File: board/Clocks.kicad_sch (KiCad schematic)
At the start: 21 parts, among them J10 Front Panel, J11 ATX-24, J5 0.89489MHz, J6 1.78977MHz, J7 3.57955MHz, J8 7.15909MHz, U39 74ACT14, U40 74F191, U43 DM1813-10, Y1 14.31818MHz

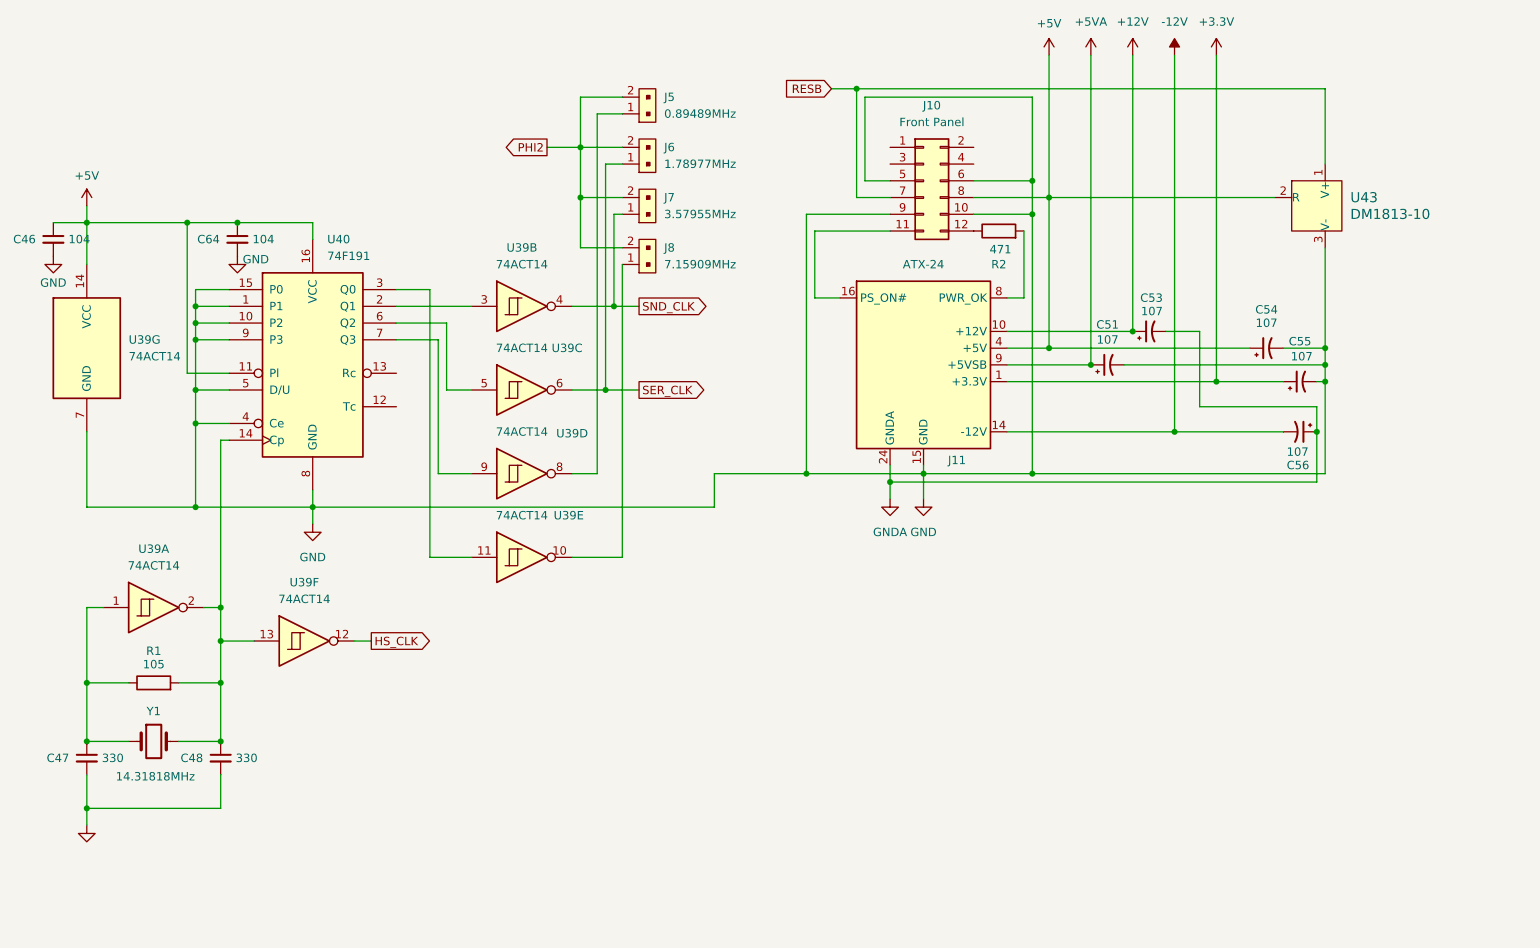
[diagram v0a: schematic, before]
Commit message: Board V1.8D: reliability changes only, the same software as 1.8C
CMOS highs into the W65C02S: U11 (its clock), U22 (IRQB) and U59 (its data bus) are 74ACT parts.
Decoupling at the sound chips and op-amps; four 47 uF bulk capacitors on +5 V; GNDA joined to GND once,
by the YM3012 (R29). Series terminations on the clocks (R23-R27, each driver's net X_SRC) and on the
crystal's drive (R22). A fixed pull-up on RDY (R28); pull-ups on the data bus (RN4: an empty slot reads
$FF). U26's spare half placed and disabled, and U22's spare inputs tied low. ATX pin 20 feeds the slots'
-5V. The ACIA's CTS through a jumper (J30: 1-2 as 1.8C, 2-3 always on). Loose wires removed, no-connects
marked, the root sheet's boxes tidied, and every sheet's revision set to 1.8D. The netlist differs from
1.8C's only by these (checked net by net); ERC finds nothing new. board/CHANGES-1.8D.md lists them. The
PCB isn't updated yet.

Co-Authored-By: Claude Opus 5.5 <noreply@anthropic.com>
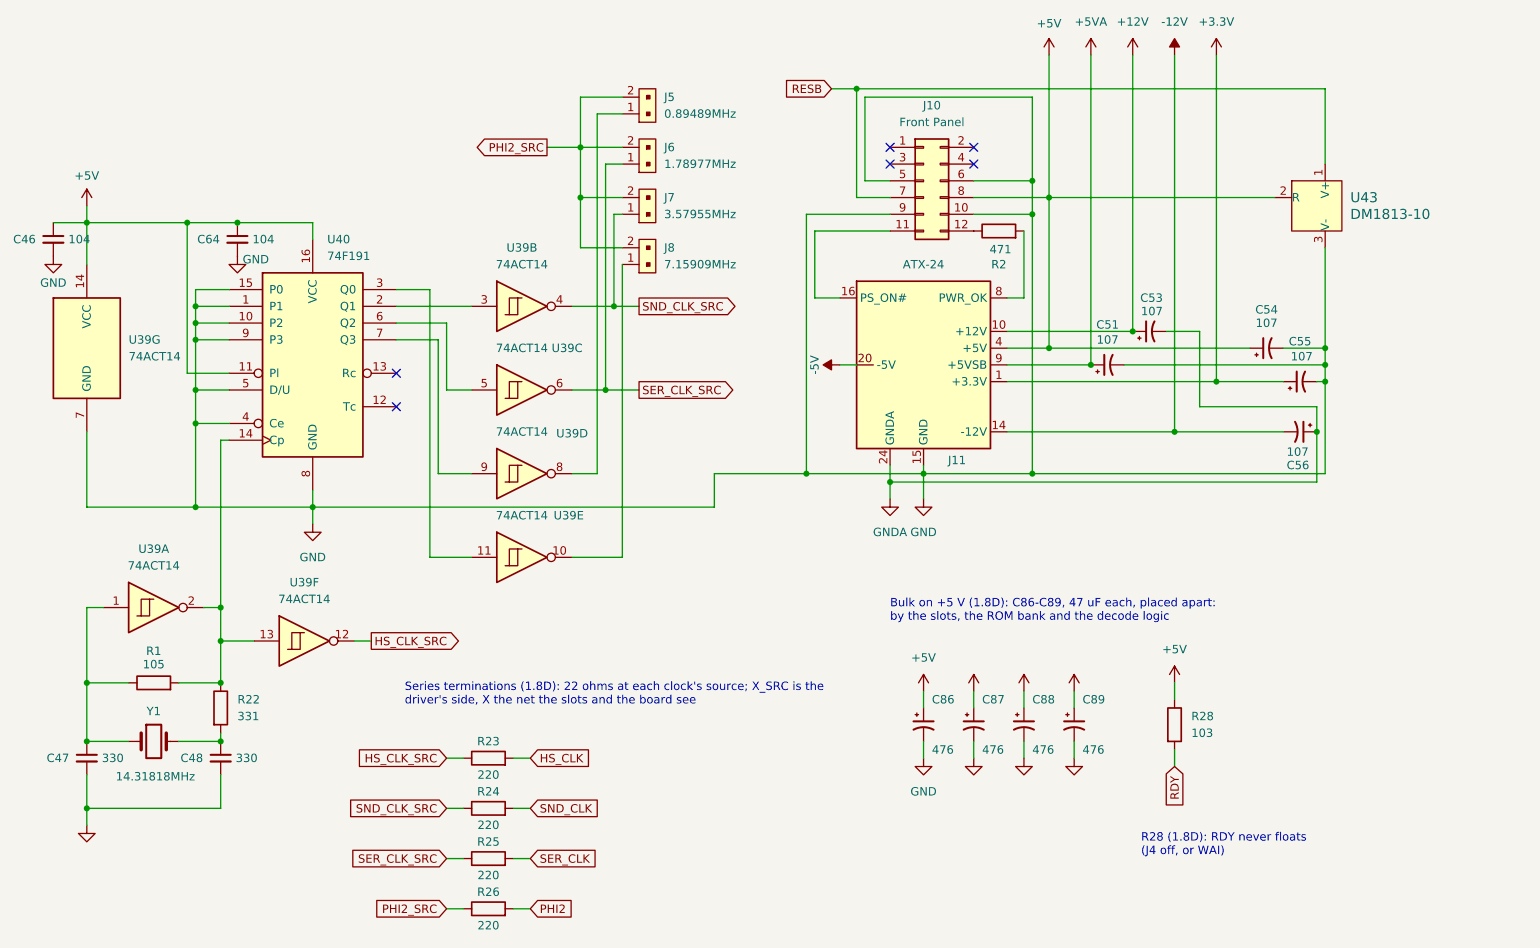
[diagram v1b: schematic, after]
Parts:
- added C86, C87, C88, C89: 476, Capacitor_THT:CP_Radial_D6.3mm_P2.50mm, symbol Device:C_Polarized_Small_US
- added R22: 331, Resistor_THT:R_Axial_DIN0204_L3.6mm_D1.6mm_P5.08mm_Horizontal, symbol Device:R
- added R23, R24, R25, R26: 220, Resistor_THT:R_Axial_DIN0204_L3.6mm_D1.6mm_P5.08mm_Horizontal, symbol Device:R
- added R28: 103, Resistor_THT:R_Axial_DIN0204_L3.6mm_D1.6mm_P5.08mm_Horizontal, symbol Device:R
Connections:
- net +5V: now also C86.1, C87.1, C88.1, C89.1, R28.1
- net GND: now also C86.2, C87.2, C88.2, C89.2
- net HS_CLK: now also R23.2; no longer U39.12
- net PHI2: now also R26.2; no longer J5.2, J6.2, J7.2, J8.2
- net SER_CLK: now also R25.2; no longer J6.1, U39.6
- net SND_CLK: now also R24.2; no longer J7.1, U39.4
- net at R1.2, U39.13, U39.2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: now also R22.1; no longer C48.1, Y1.2
- net -5V: now reaches J11.20 (-5V)
- new net: C48.1, R22.2, Y1.2
- new net HS_CLK_SRC: R23.1, U39.12
- new net PHI2_SRC: J5.2, J6.2, J7.2, J8.2, R26.1
- new net RDY: R28.2
- new net SER_CLK_SRC: J6.1, R25.1, U39.6
- new net SND_CLK_SRC: J7.1, R24.1, U39.4
- no-connect marks 0 -> 6
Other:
- note added: "Bulk on +5 V (1.8D): C86-C89, 47 uF each, placed apart: by the slots, the ROM bank and the decode logic"
- note added: "R28 (1.8D): RDY never floats (J4 off, or WAI)"
- note added: "Series terminations (1.8D): 22 ohms at each clock's source; X_SRC is the driver's side, X the net the slots and the board see"

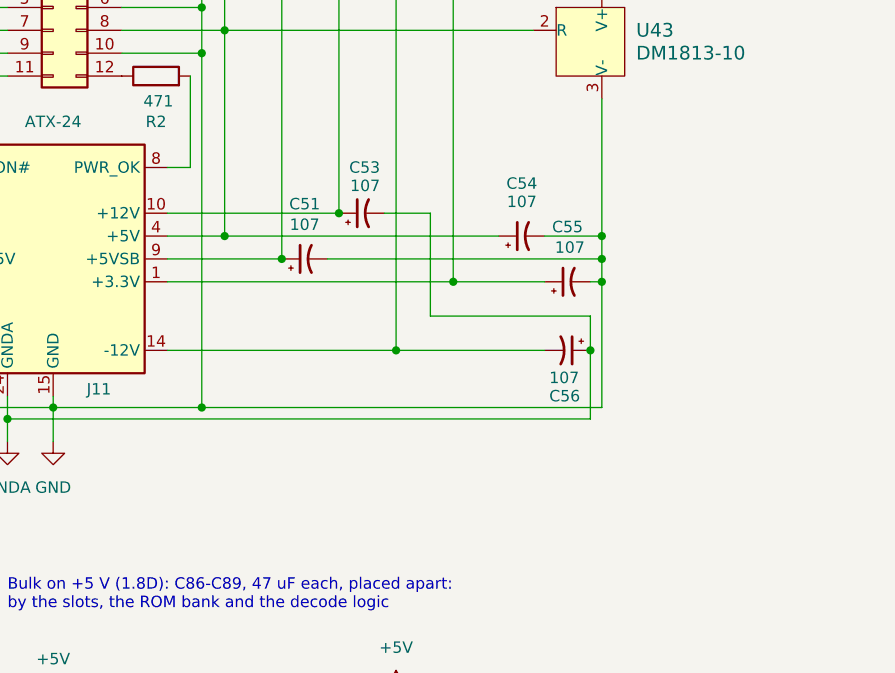
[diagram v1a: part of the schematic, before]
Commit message: Board V1.8D: the power LED (J10 pin 12, R2) lit from +5 V, not from the ATX supply's PWR_OK
PWR_OK is a logic signal; the main +5 V rail is up only while the supply is on, so the LED means the same.
PWR_OK is marked unconnected. The netlist's only change: R2 pin 2 from PWR_OK to +5V.

Co-Authored-By: Claude Opus 5.5 <noreply@anthropic.com>
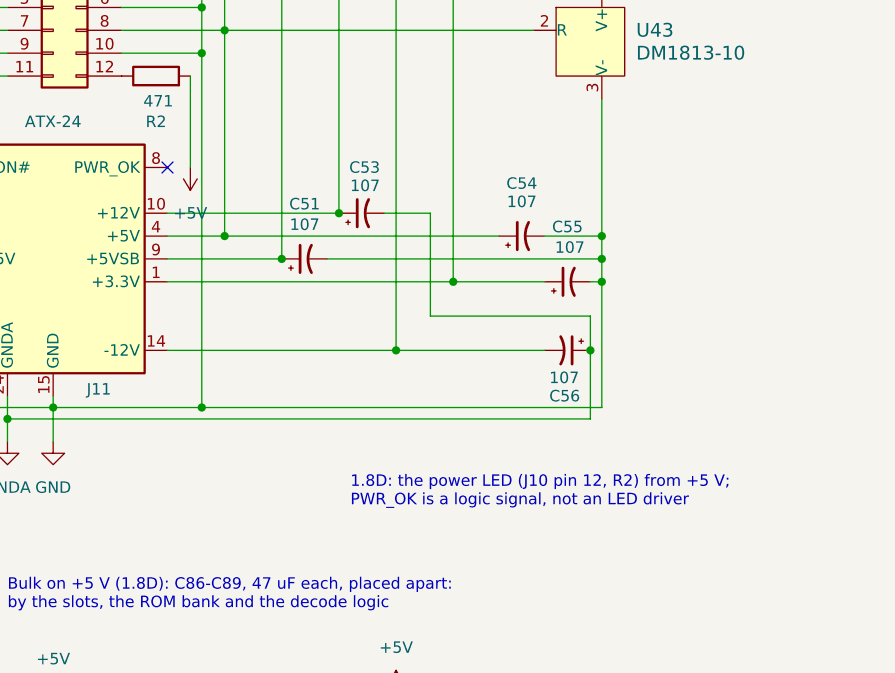
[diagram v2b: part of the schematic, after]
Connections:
- net +5V: now also R2.2
- net at J11.8 (PWR_OK): no longer R2.2
- no-connect marks 6 -> 7
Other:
- note added: "1.8D: the power LED (J10 pin 12, R2) from +5 V; PWR_OK is a logic signal, not an LED driver"
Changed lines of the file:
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@@
 	(wire
 		(pts
-			(xy 185.42 82.55) (xy 187.96 82.55)
-		)
-		(stroke
-			(width 0)
-			(type default)
-		)
-	)
-	(wire
-		(pts
 			(xy 99.06 109.22) (xy 104.14 109.22)
 		)
@@
 	(no_connect (at 167.64 62.23))
 	(no_connect (at 180.34 62.23))
+	(symbol
+		(lib_id "power:+5V")
+		(at 187.96 82.55 180)
+		(unit 1)
+		(exclude_from_sim no)
+		(in_bom yes)
+		(on_board yes)
+		(dnp no)
+		(property "Reference" "#PWR0111"
+			(at 187.96 82.55 0)
+			(effects
+				(font (size 1.27 1.27))
+				hide
+			)
+		)
+		(property "Value" "+5V"
+			(at 187.96 87.63 0)
+			(effects
+				(font (size 1.27 1.27))
+			)
+		)
+		(property "Footprint" ""
+			(at 187.96 82.55 0)
+			(effects
+				(font (size 1.27 1.27))
+				hide
+			)
+		)
+		(property "Datasheet" ""
+			(at 187.96 82.55 0)
+			(effects
+				(font (size 1.27 1.27))
+				hide
+			)
+		)
+		(pin "1")
+		(instances
+			(project ""
+				(path "/ef29fc71-3fec-48b5-8a1a-46bee537a98c/9a593a77-f18f-43cb-9fdd-893618b7b90a"
+					(reference "#PWR0111")
+					(unit 1)
+				)
+			)
+		)
+	)
+	(no_connect (at 185.42 82.55))
+	(text "1.8D: the power LED (J10 pin 12, R2) from +5 V;\nPWR_OK is a logic signal, not an LED driver"
+		(exclude_from_sim no)
+		(at 205.74 116.84 0)
+		(effects
+			(font (size 1.27 1.27))
+			(justify left top)
+		)
+	)
 )
